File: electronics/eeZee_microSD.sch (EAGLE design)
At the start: 12 parts, among them U1 MCP1824S, U2 74HC4050, U4 MICROSD_CD

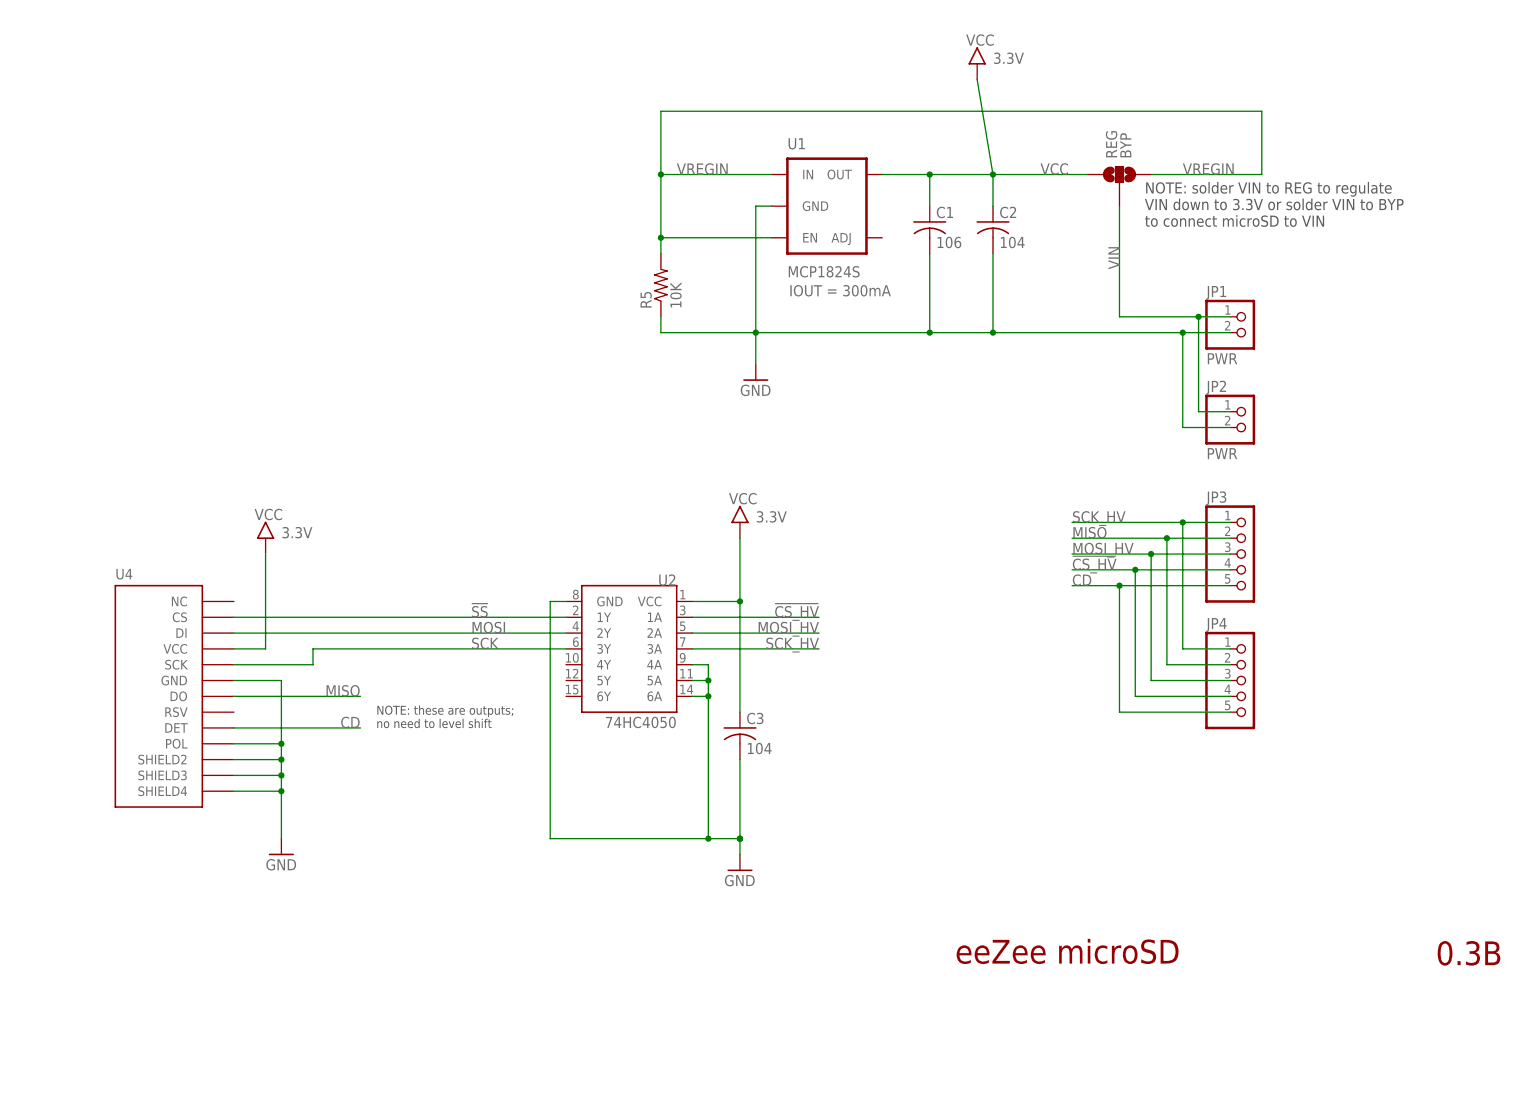
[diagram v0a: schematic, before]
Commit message: new regulator
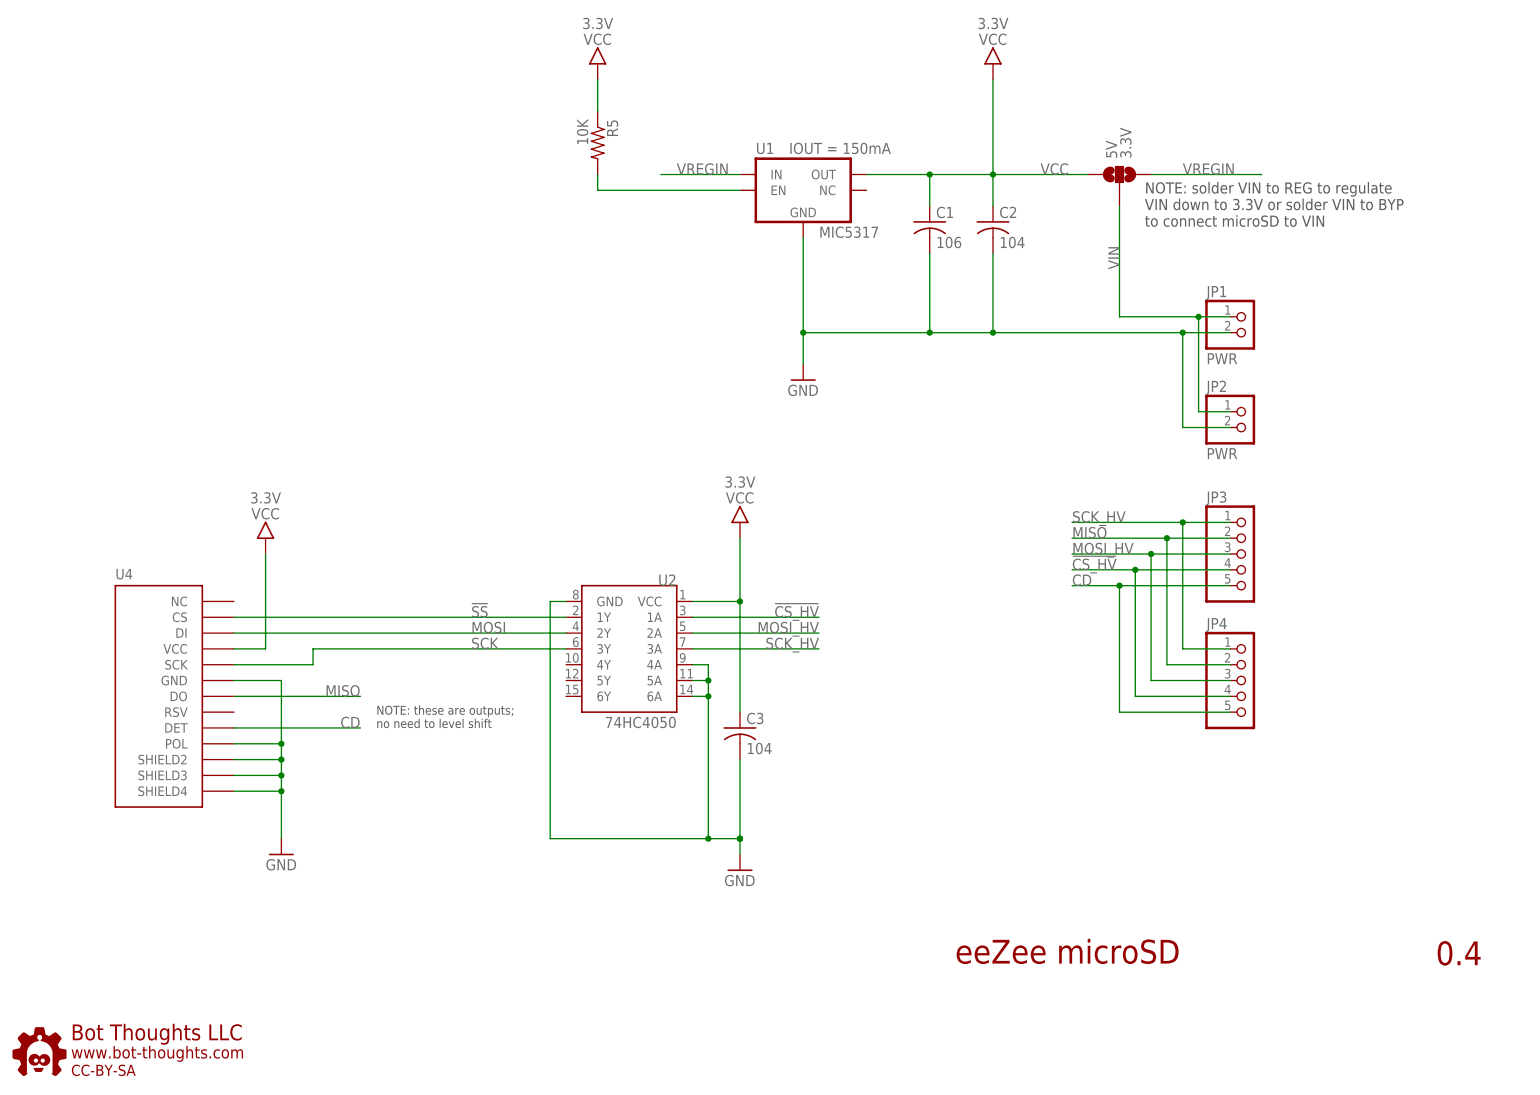
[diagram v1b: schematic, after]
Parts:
- added U$5: BTLOGO-LOGO-SM, bt:BTLOGO-LOGO-SM
- 5V: value BYP -> 3.3V
- U1: value MCP1824S -> MIC5317; device mes_regulators:MCP1824 -> bt_regulator:MIC5317; IOUT 300mA -> 150mA; PARTNO MCP1824ST-3302E/DB -> MIC5317-3.3YM5-TR
- renumbered REG to 5V
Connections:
- new net EN: R5.2, U1.EN
- net GND: no longer R5.1
- net VCC: now also R5.1
- net VREGIN: no longer R5.2, U1.EN
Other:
- note added: "0.4"
- note removed: "0.3B"
- moved on the sheet: R5

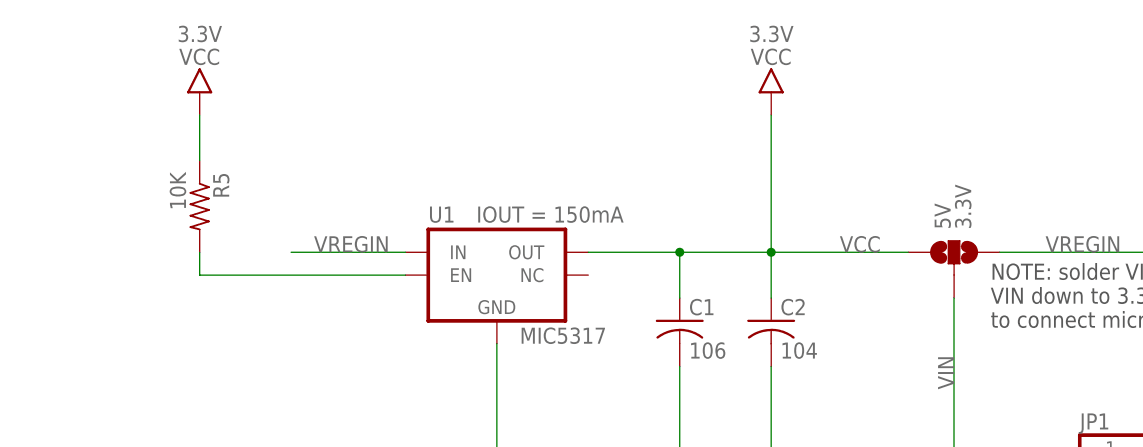
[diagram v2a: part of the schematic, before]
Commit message: finished routing, silk, added instructions and help url
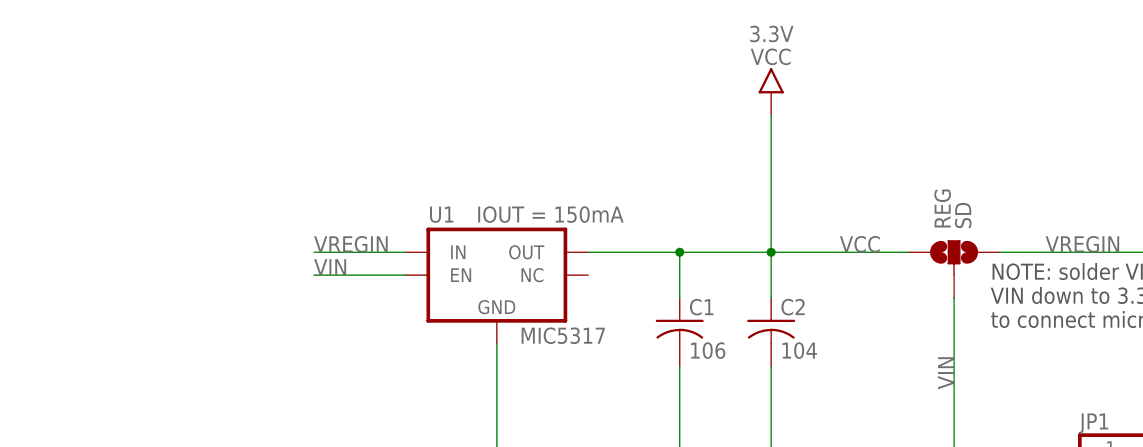
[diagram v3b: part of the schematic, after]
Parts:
- removed R5: 10K, rcl:R-US_R0603
- REG: value 3.3V -> SD
- renumbered 5V to REG
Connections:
- removed net EN: R5.2, U1.EN
- net VCC: no longer R5.1
- net VIN: now also U1.EN
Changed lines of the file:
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@@
 <attribute name="PARTNO" value="LMK107B7105KA-T"/>
 </part>
-<part name="5V" library="SparkFun" deviceset="SOLDERJUMPER_2WAY" device="S" value="3.3V"/>
+<part name="REG" library="SparkFun" deviceset="SOLDERJUMPER_2WAY" device="S" value="SD"/>
 <part name="FRAME1" library="mes" deviceset="LETTER_L" device=""/>
-<part name="R5" library="rcl" deviceset="R-US_" device="R0603" value="10K">
-<attribute name="PARTNO" value="ERJ-3GEYJ103V"/>
-</part>
 <part name="GND2" library="mes" deviceset="GND" device=""/>
 <part name="U2" library="SparkFun" deviceset="HEX_CONVERTER" device="" value="74HC4050"/>
@@
 <part name="JP3" library="pinhead-2" deviceset="PINHD-1X05" device="_2.54-S"/>
 <part name="U4" library="bt_electromech" deviceset="MICROSD_CD" device=""/>
-<part name="U$1" library="bt" deviceset="VCC" device="" value="3.3V"/>
 <part name="U$5" library="bt" deviceset="BTLOGO" device="-LOGO-SM" value="BTLOGO-LOGO-SM"/>
 </parts>
@@
 <attribute name="PARTNO" value="JMK212BJ226MG-T" x="149.86" y="142.24" size="1.778" layer="96" display="off"/>
 </instance>
-<instance part="5V" gate="G$1" x="180.34" y="149.86" rot="R90"/>
+<instance part="REG" gate="G$1" x="180.34" y="149.86" rot="R90"/>
 <instance part="FRAME1" gate="G$1" x="0" y="0"/>
 <instance part="FRAME1" gate="G$2" x="147.32" y="2.54"/>
-<instance part="R5" gate="G$1" x="96.52" y="154.94" rot="R270">
-<attribute name="PARTNO" value="ERJ-3GEYJ102V" x="96.52" y="154.94" size="1.778" layer="96" rot="R270" display="off"/>
-</instance>
 <instance part="GND2" gate="1" x="129.54" y="116.84"/>
 <instance part="U2" gate="G$1" x="101.6" y="73.66" rot="MR0"/>
@@
 <instance part="JP3" gate="A" x="200.66" y="88.9"/>
 <instance part="U4" gate="U1" x="25.4" y="66.04"/>
-<instance part="U$1" gate="G$1" x="96.52" y="165.1"/>
 <instance part="U$5" gate="G$1" x="2.54" y="5.08"/>
 </instances>
@@
 <net name="VREGIN" class="0">
 <segment>
-<pinref part="5V" gate="G$1" pin="3"/>
+<pinref part="REG" gate="G$1" pin="3"/>
 <wire x1="203.2" y1="149.86" x2="185.42" y2="149.86" width="0.1524" layer="91"/>
 <label x="190.5" y="149.86" size="1.778" layer="95"/>
@@
 <segment>
 <pinref part="U1" gate="U1" pin="IN"/>
-<wire x1="106.68" y1="149.86" x2="119.38" y2="149.86" width="0.1524" layer="91"/>
+<wire x1="109.22" y1="149.86" x2="119.38" y2="149.86" width="0.1524" layer="91"/>
 <label x="109.22" y="149.86" size="1.778" layer="95"/>
 </segment>
@@
 <net name="VIN" class="0">
 <segment>
-<pinref part="5V" gate="G$1" pin="2"/>
+<pinref part="REG" gate="G$1" pin="2"/>
 <wire x1="180.34" y1="144.78" x2="180.34" y2="127" width="0.1524" layer="91"/>
 <pinref part="JP1" gate="A" pin="1"/>
@@
 <junction x="193.04" y="127"/>
 </segment>
+<segment>
+<pinref part="U1" gate="U1" pin="EN"/>
+<wire x1="119.38" y1="147.32" x2="109.22" y2="147.32" width="0.1524" layer="91"/>
+<label x="109.22" y="147.32" size="1.778" layer="95"/>
+</segment>
 </net>
 <net name="!CS_HV" class="0">
@@
 <pinref part="C1" gate="G$1" pin="1"/>
 <junction x="149.86" y="149.86"/>
-<pinref part="5V" gate="G$1" pin="1"/>
+<pinref part="REG" gate="G$1" pin="1"/>
 <wire x1="149.86" y1="149.86" x2="160.02" y2="149.86" width="0.1524" layer="91"/>
 <label x="167.64" y="149.86" size="1.778" layer="95"/>
@@
 <pinref part="U4" gate="U1" pin="VCC"/>
 </segment>
-<segment>
-<pinref part="R5" gate="G$1" pin="1"/>
-<pinref part="U$1" gate="G$1" pin="VCC"/>
-<wire x1="96.52" y1="165.1" x2="96.52" y2="160.02" width="0.1524" layer="91"/>
-</segment>
 </net>
 <net name="CD" class="0">
@@
 </segment>
 </net>
-<net name="EN" class="0">
-<segment>
-<pinref part="U1" gate="U1" pin="EN"/>
-<wire x1="119.38" y1="147.32" x2="96.52" y2="147.32" width="0.1524" layer="91"/>
-<pinref part="R5" gate="G$1" pin="2"/>
-<wire x1="96.52" y1="149.86" x2="96.52" y2="147.32" width="0.1524" layer="91"/>
-</segment>
-</net>

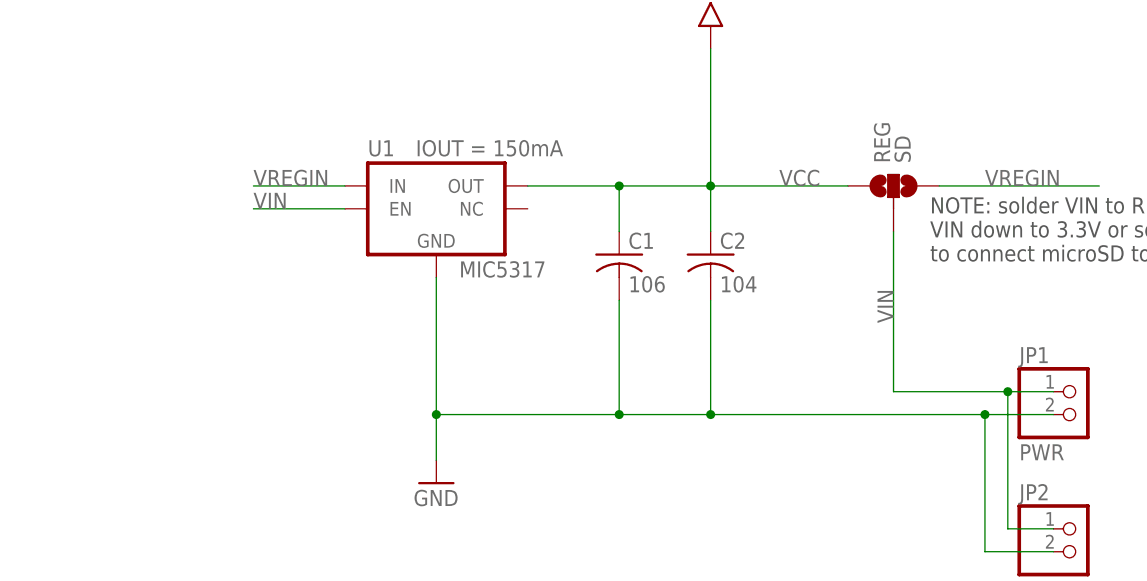
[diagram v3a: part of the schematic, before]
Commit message: fixed input/output caps per datasheet, changed DET to CD on silk
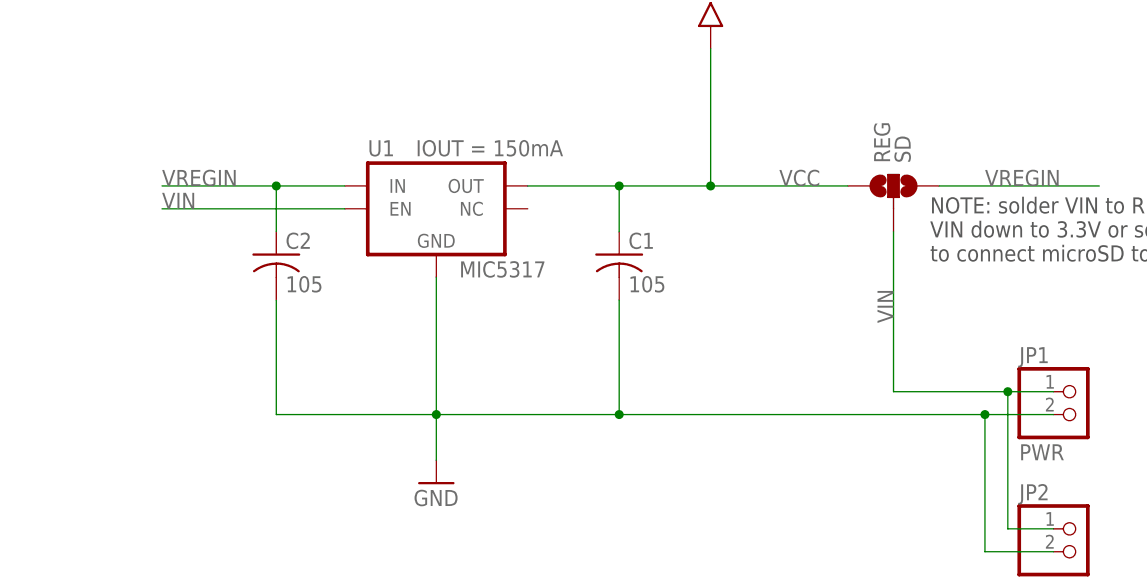
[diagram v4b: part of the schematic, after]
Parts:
- C1: value 106 -> 105; device rcl:C-USC1206 -> bt_rcl:C-0603
- C2: value 104 -> 105; device rcl:C-USC0603 -> bt_rcl:C-0603
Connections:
- net GND: now also C1.-, C2.-; no longer C1.2, C2.2
- net VCC: now also C1.+; no longer C1.1, C2.1
- net VREGIN: now also C2.+
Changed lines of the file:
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@@
 <attribute name="VOUT" value="3.3V"/>
 </part>
-<part name="C1" library="rcl" deviceset="C-US" device="C1206" value="106">
+<part name="C1" library="bt_rcl" deviceset="C" device="-0603" value="105">
 <attribute name="PARTNO" value="LMK107B7105KA-T"/>
 </part>
@@
 <part name="GND2" library="mes" deviceset="GND" device=""/>
 <part name="U2" library="SparkFun" deviceset="HEX_CONVERTER" device="" value="74HC4050"/>
-<part name="C2" library="rcl" deviceset="C-US" device="C0603" value="104">
-<attribute name="PARTNO" value="LMK107B7105KA-T"/>
-</part>
 <part name="C3" library="rcl" deviceset="C-US" device="C0603" value="104">
 <attribute name="PARTNO" value="LMK107B7105KA-T"/>
@@
 <part name="U4" library="bt_electromech" deviceset="MICROSD_CD" device=""/>
 <part name="U$5" library="bt" deviceset="BTLOGO" device="-LOGO-SM" value="BTLOGO-LOGO-SM"/>
+<part name="C2" library="bt_rcl" deviceset="C" device="-0603" value="105">
+<attribute name="PARTNO" value="LMK107B7105KA-T"/>
+</part>
 </parts>
 <sheets>
@@
 <attribute name="IOUT" x="127.254" y="153.162" size="1.778" layer="96" display="both"/>
 </instance>
-<instance part="C1" gate="G$1" x="149.86" y="142.24">
+<instance part="C1" gate="C1" x="149.86" y="142.24">
 <attribute name="PARTNO" value="JMK212BJ226MG-T" x="149.86" y="142.24" size="1.778" layer="96" display="off"/>
 </instance>
@@
 <instance part="GND2" gate="1" x="129.54" y="116.84"/>
 <instance part="U2" gate="G$1" x="101.6" y="73.66" rot="MR0"/>
-<instance part="C2" gate="G$1" x="160.02" y="142.24">
-<attribute name="PARTNO" value="JMK212BJ226MG-T" x="160.02" y="142.24" size="1.778" layer="96" display="off"/>
-</instance>
 <instance part="C3" gate="G$1" x="119.38" y="60.96">
 <attribute name="PARTNO" value="JMK212BJ226MG-T" x="119.38" y="60.96" size="1.778" layer="96" display="off"/>
@@
 <instance part="U4" gate="U1" x="25.4" y="66.04"/>
 <instance part="U$5" gate="G$1" x="2.54" y="5.08"/>
+<instance part="C2" gate="C1" x="111.76" y="142.24">
+<attribute name="PARTNO" value="JMK212BJ226MG-T" x="111.76" y="142.24" size="1.778" layer="96" display="off"/>
+</instance>
 </instances>
 <busses>
@@
 </segment>
 <segment>
-<wire x1="160.02" y1="124.46" x2="149.86" y2="124.46" width="0.1524" layer="91"/>
 <wire x1="149.86" y1="124.46" x2="129.54" y2="124.46" width="0.1524" layer="91"/>
 <pinref part="U1" gate="U1" pin="GND"/>
 <wire x1="129.54" y1="139.7" x2="129.54" y2="124.46" width="0.1524" layer="91"/>
 <junction x="129.54" y="124.46"/>
-<pinref part="C1" gate="G$1" pin="2"/>
+<pinref part="C1" gate="C1" pin="-"/>
 <wire x1="149.86" y1="137.16" x2="149.86" y2="124.46" width="0.1524" layer="91"/>
 <junction x="149.86" y="124.46"/>
 <pinref part="GND2" gate="1" pin="GND"/>
 <wire x1="129.54" y1="119.38" x2="129.54" y2="124.46" width="0.1524" layer="91"/>
-<pinref part="C2" gate="G$1" pin="2"/>
-<wire x1="160.02" y1="137.16" x2="160.02" y2="124.46" width="0.1524" layer="91"/>
-<junction x="160.02" y="124.46"/>
 <pinref part="JP1" gate="A" pin="2"/>
 <wire x1="198.12" y1="124.46" x2="190.5" y2="124.46" width="0.1524" layer="91"/>
 <pinref part="JP2" gate="A" pin="2"/>
-<wire x1="190.5" y1="124.46" x2="160.02" y2="124.46" width="0.1524" layer="91"/>
+<wire x1="190.5" y1="124.46" x2="149.86" y2="124.46" width="0.1524" layer="91"/>
 <wire x1="198.12" y1="109.22" x2="190.5" y2="109.22" width="0.1524" layer="91"/>
 <wire x1="190.5" y1="109.22" x2="190.5" y2="124.46" width="0.1524" layer="91"/>
 <junction x="190.5" y="124.46"/>
+<pinref part="C2" gate="C1" pin="-"/>
+<wire x1="129.54" y1="124.46" x2="111.76" y2="124.46" width="0.1524" layer="91"/>
+<wire x1="111.76" y1="124.46" x2="111.76" y2="137.16" width="0.1524" layer="91"/>
 </segment>
 </net>
@@
 <segment>
 <pinref part="U1" gate="U1" pin="IN"/>
-<wire x1="109.22" y1="149.86" x2="119.38" y2="149.86" width="0.1524" layer="91"/>
-<label x="109.22" y="149.86" size="1.778" layer="95"/>
+<wire x1="99.06" y1="149.86" x2="111.76" y2="149.86" width="0.1524" layer="91"/>
+<label x="99.06" y="149.86" size="1.778" layer="95"/>
+<pinref part="C2" gate="C1" pin="+"/>
+<wire x1="111.76" y1="149.86" x2="119.38" y2="149.86" width="0.1524" layer="91"/>
+<wire x1="111.76" y1="144.78" x2="111.76" y2="149.86" width="0.1524" layer="91"/>
+<junction x="111.76" y="149.86"/>
 </segment>
 </net>
@@
 <segment>
 <pinref part="U1" gate="U1" pin="EN"/>
-<wire x1="119.38" y1="147.32" x2="109.22" y2="147.32" width="0.1524" layer="91"/>
-<label x="109.22" y="147.32" size="1.778" layer="95"/>
+<wire x1="119.38" y1="147.32" x2="99.06" y2="147.32" width="0.1524" layer="91"/>
+<label x="99.06" y="147.32" size="1.778" layer="95"/>
 </segment>
 </net>
@@
 <wire x1="139.7" y1="149.86" x2="149.86" y2="149.86" width="0.1524" layer="91"/>
 <wire x1="149.86" y1="144.78" x2="149.86" y2="149.86" width="0.1524" layer="91"/>
-<pinref part="C1" gate="G$1" pin="1"/>
+<pinref part="C1" gate="C1" pin="+"/>
 <junction x="149.86" y="149.86"/>
 <pinref part="REG" gate="G$1" pin="1"/>
@@
 <wire x1="160.02" y1="149.86" x2="175.26" y2="149.86" width="0.1524" layer="91"/>
 <junction x="160.02" y="149.86"/>
-<pinref part="C2" gate="G$1" pin="1"/>
-<wire x1="160.02" y1="144.78" x2="160.02" y2="149.86" width="0.1524" layer="91"/>
 <pinref part="U$2" gate="G$1" pin="VCC"/>
 <wire x1="160.02" y1="149.86" x2="160.02" y2="165.1" width="0.1524" layer="91"/>
